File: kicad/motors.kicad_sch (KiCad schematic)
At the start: 18 parts, among them U1 DRV8848, U2 DRV8848, U3 DRV8848

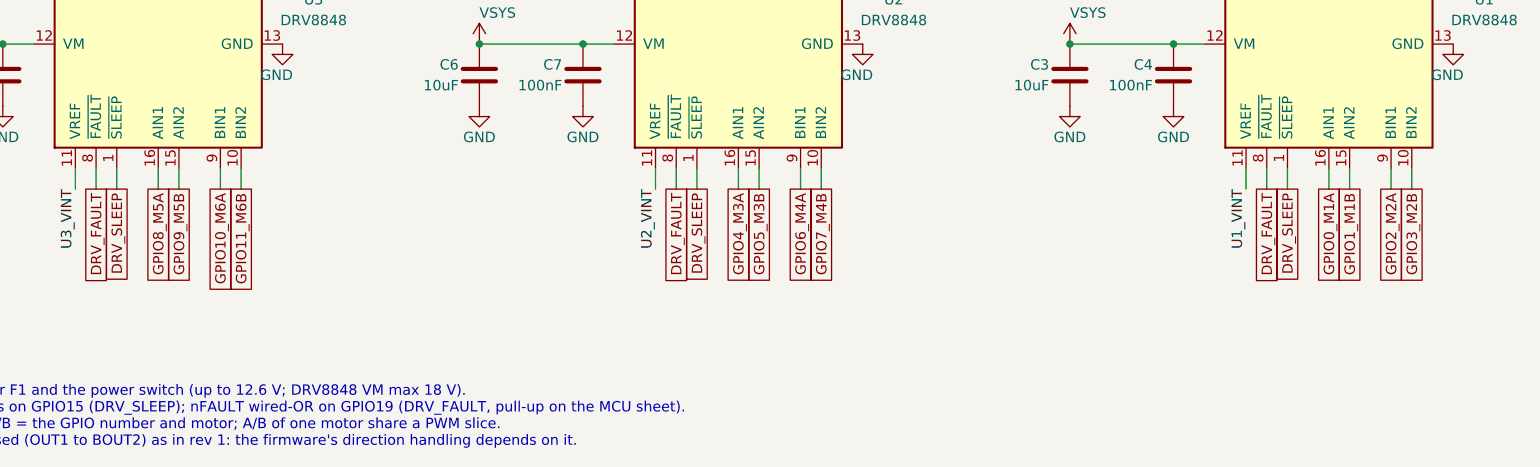
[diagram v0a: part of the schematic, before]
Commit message: Lay out rev 2 with an internal pack, protector and cost-down parts
Board is 91 x 47 mm for a 96 x 52 mm enclosure, with placement and hand
power routing done; signal routing is still to do.

- Internal Gens Ace 3S 1000 mAh pack on an XT60 pigtail, protected on the
  board by a BQ7791501 with back-to-back low-side FETs and a 2.5 mOhm
  shunt, plus a balance header and two NTCs.
- USB-A and USB-C on the top edge, IO as a recessed 3 x 6 pin block, GPIO
  map re-swapped for the placement, USB nets renamed with P/N suffixes
  for the diff-pair router.
- Cost-down swaps that keep every feature: basic or preferred passives
  and ICs, cheaper connectors, a THT power switch rated for 12.6 V, and
  replacements for the low-stock TH1 and Q2/Q3. L3 is Digi-Key sourced
  and hand-placed.
- Net classes and design rules, rev 2 power-net widths in review.py, and
  the PCB critic and loop updated for rev 2.

Schematic review passes; PCB review passes every gate except unrouted.

Co-Authored-By: Claude Opus 5.5 <noreply@anthropic.com>
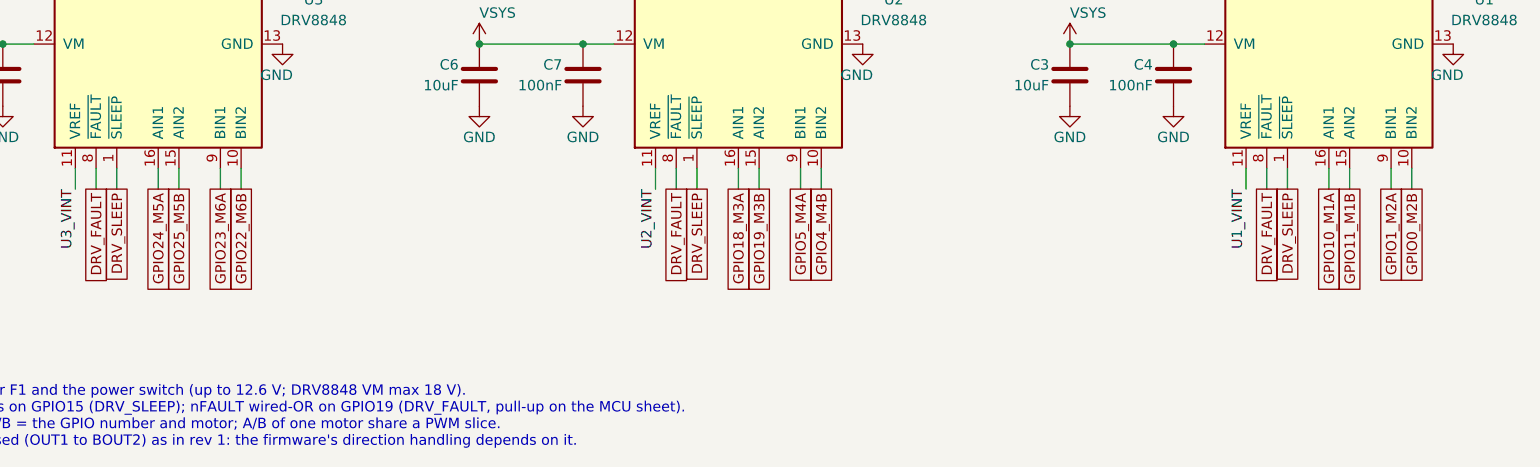
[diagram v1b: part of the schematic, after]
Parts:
- C13, C2, C9: footprint Capacitor_SMD:C_0805_2012Metric -> Capacitor_SMD:C_0603_1608Metric; LCSC Part # C377773 -> C23630; MPN CL21A225KBQNNNE -> CL10A225KO8NNNC
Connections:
- net GPIO0_M1A renamed GPIO10_M1A
- net GPIO10_M6A renamed GPIO23_M6A
- net GPIO11_M6B renamed GPIO22_M6B
- net GPIO1_M1B renamed GPIO11_M1B
- net GPIO2_M2A renamed GPIO1_M2A
- net GPIO3_M2B renamed GPIO0_M2B
- net GPIO4_M3A renamed GPIO18_M3A
- net GPIO5_M3B renamed GPIO19_M3B
- net GPIO6_M4A renamed GPIO5_M4A
- net GPIO7_M4B renamed GPIO4_M4B
- net GPIO8_M5A renamed GPIO24_M5A
- net GPIO9_M5B renamed GPIO25_M5B
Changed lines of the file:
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@@
 			)
 		)
-		(property "Footprint" "Capacitor_SMD:C_0805_2012Metric"
+		(property "Footprint" "Capacitor_SMD:C_0603_1608Metric"
 			(at 219.71 37.795199999999994 0)
 			(effects
@@
 			)
 		)
-		(property "LCSC Part #" "C377773"
+		(property "LCSC Part #" "C23630"
 			(at 251.4601 -187.9601 0)
 			(effects
@@
 			)
 		)
-    (property "MPN" "CL21A225KBQNNNE" (at 223.52 36.83 0)
+    (property "MPN" "CL10A225KO8NNNC" (at 223.52 36.83 0)
       (effects (font (size 1.27 1.27)) (hide yes))
     )
@@
 			)
 		)
-		(property "Footprint" "Capacitor_SMD:C_0805_2012Metric"
+		(property "Footprint" "Capacitor_SMD:C_0603_1608Metric"
 			(at 147.32 37.795199999999994 0)
 			(effects
@@
 			)
 		)
-		(property "LCSC Part #" "C377773"
+		(property "LCSC Part #" "C23630"
 			(at 179.0701 -115.5701 0)
 			(effects
@@
 			)
 		)
-    (property "MPN" "CL21A225KBQNNNE" (at 151.13 36.83 0)
+    (property "MPN" "CL10A225KO8NNNC" (at 151.13 36.83 0)
       (effects (font (size 1.27 1.27)) (hide yes))
     )
@@
 			)
 		)
-		(property "Footprint" "Capacitor_SMD:C_0805_2012Metric"
+		(property "Footprint" "Capacitor_SMD:C_0603_1608Metric"
 			(at 76.2 37.795199999999994 0)
 			(effects
@@
 			)
 		)
-		(property "LCSC Part #" "C377773"
+		(property "LCSC Part #" "C23630"
 			(at 107.9501 -44.450100000000006 0)
 			(effects
@@
 			)
 		)
-    (property "MPN" "CL21A225KBQNNNE" (at 80.01 36.83 0)
+    (property "MPN" "CL10A225KO8NNNC" (at 80.01 36.83 0)
       (effects (font (size 1.27 1.27)) (hide yes))
     )
@@
 	)
 	(embedded_fonts no)
-	(global_label "GPIO0_M1A"
+	(global_label "GPIO10_M1A"
 		(at 238.76 69.85 270)
 		(effects
@@
 		)
 	)
-	(global_label "GPIO1_M1B"
+	(global_label "GPIO11_M1B"
 		(at 241.3 69.85 270)
 		(effects
@@
 		)
 	)
-	(global_label "GPIO2_M2A"
+	(global_label "GPIO1_M2A"
 		(at 246.38 69.85 270)
 		(effects
@@
 		)
 	)
-	(global_label "GPIO3_M2B"
+	(global_label "GPIO0_M2B"
 		(at 248.92 69.85 270)
 		(effects
@@
 		)
 	)
-	(global_label "GPIO4_M3A"
+	(global_label "GPIO18_M3A"
 		(at 166.37 69.85 270)
 		(effects
@@
 		)
 	)
-	(global_label "GPIO5_M3B"
+	(global_label "GPIO19_M3B"
 		(at 168.91 69.85 270)
 		(effects
@@
 		)
 	)
-	(global_label "GPIO6_M4A"
+	(global_label "GPIO5_M4A"
 		(at 173.99 69.85 270)
 		(effects
@@
 		)
 	)
-	(global_label "GPIO7_M4B"
+	(global_label "GPIO4_M4B"
 		(at 176.53 69.85 270)
 		(effects
@@
 		)
 	)
-	(global_label "GPIO8_M5A"
+	(global_label "GPIO24_M5A"
 		(at 95.25 69.85 270)
 		(effects
@@
 		)
 	)
-	(global_label "GPIO9_M5B"
+	(global_label "GPIO25_M5B"
 		(at 97.79 69.85 270)
 		(effects
@@
 		)
 	)
-	(global_label "GPIO10_M6A"
+	(global_label "GPIO23_M6A"
 		(at 102.87 69.85 270)
 		(effects
@@
 		)
 	)
-	(global_label "GPIO11_M6B"
+	(global_label "GPIO22_M6B"
 		(at 105.41 69.85 270)
 		(effects

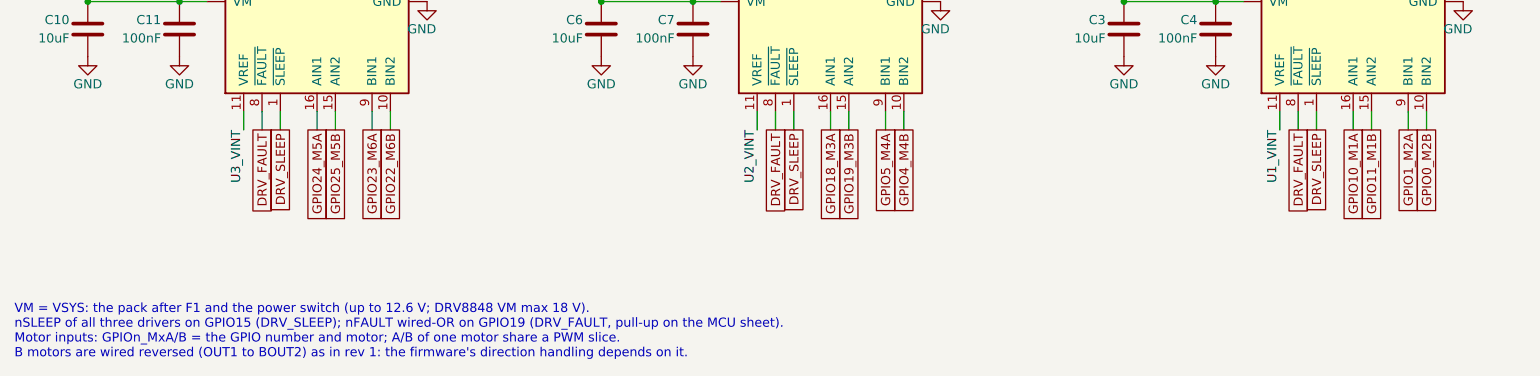
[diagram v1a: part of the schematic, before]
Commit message: Re-lay out rev 2 around an Ovonic 450 pack on top of the board
The internal pack is now an Ovonic 3S 450 mAh XT30 pack sitting 2 mm
above the board over the low-power logic area, on an XT30 pigtail. The
board is 88.5 x 47 mm with 2 mm corner radii, for a box of about
93.5 x 52 x 24.6 mm whose face has no openings.

- IO S1-S6 are a 3 x 6 right-angle header out of the left end, beside
  M5/M6, replacing the recessed vertical block.
- BOOT is a side-push switch on the top edge behind a pinhole sized for
  a 2.5 mm hex key; RESET is removed, with RUN on a bottom test pad
  beside SWCLK/SWDIO/GND.
- The CHG LED is a side-view part on the top edge; the GPIO status LED
  is removed now that the WS2812B stick shows status.
- The pack NTC is removed (a fixed 10k holds the charger's TS at 25 C);
  the protector's on-board TH1 stays.
- Q1, F1 and the other warm parts moved out from under the pack, and the
  GPIO map was re-swapped for the new placement (I2C on I2C1).

Schematic review passes; PCB review passes every gate except unrouted.

Co-Authored-By: Claude Opus 5.5 <noreply@anthropic.com>
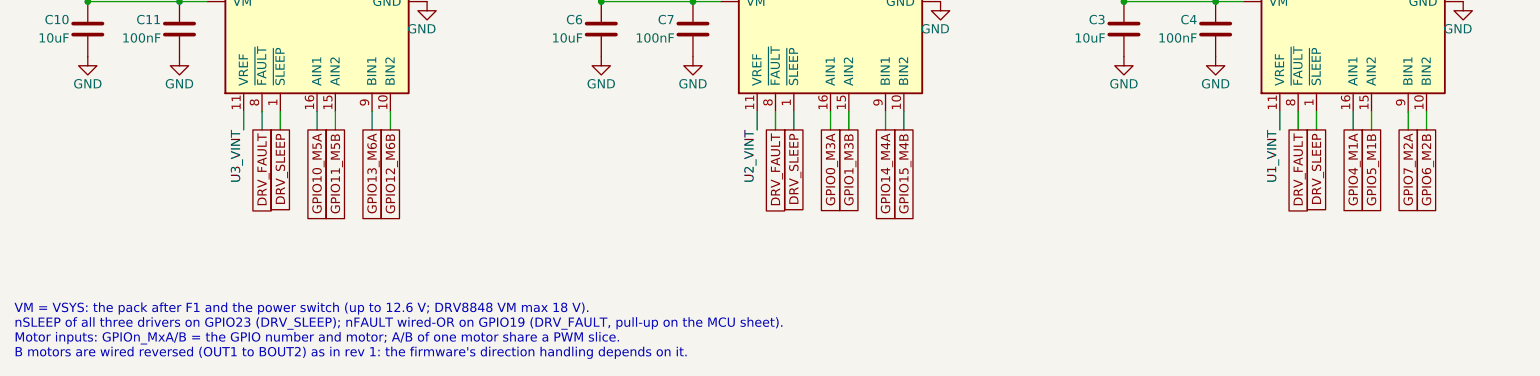
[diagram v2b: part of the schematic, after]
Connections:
- net GPIO0_M2B renamed GPIO6_M2B
- net GPIO10_M1A renamed GPIO4_M1A
- net GPIO11_M1B renamed GPIO5_M1B
- net GPIO18_M3A renamed GPIO0_M3A
- net GPIO19_M3B renamed GPIO1_M3B
- net GPIO1_M2A renamed GPIO7_M2A
- net GPIO22_M6B renamed GPIO12_M6B
- net GPIO23_M6A renamed GPIO13_M6A
- net GPIO24_M5A renamed GPIO10_M5A
- net GPIO25_M5B renamed GPIO11_M5B
- net GPIO4_M4B renamed GPIO15_M4B
- net GPIO5_M4A renamed GPIO14_M4A
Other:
- note added: "VM = VSYS: the pack after F1 and the power switch (up to 12.6 V; DRV8848 VM max 18 V). nSLEEP of all three drivers on GPIO23 (DRV_SLEEP); nFAULT wired-OR on GPIO19 (DRV_FAULT, pull-up on the MCU sheet). Motor inputs: GPIOn_MxA/B = the GPIO number and motor; A/B of one motor share a PWM slice. B motors are wired reversed (OUT1 to BOUT2) as in rev 1: the firmware's direction handling depends on it."
- note removed: "VM = VSYS: the pack after F1 and the power switch (up to 12.6 V; DRV8848 VM max 18 V). nSLEEP of all three drivers on GPIO15 (DRV_SLEEP); nFAULT wired-OR on GPIO19 (DRV_FAULT, pull-up on the MCU sheet). Motor inputs: GPIOn_MxA/B = the GPIO number and motor; A/B of one motor share a PWM slice. B motors are wired reversed (OUT1 to BOUT2) as in rev 1: the firmware's direction handling depends on it."
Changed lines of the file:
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@@
 	)
 	(embedded_fonts no)
-	(global_label "GPIO10_M1A"
+	(global_label "GPIO4_M1A"
 		(at 238.76 69.85 270)
 		(effects
@@
 		)
 	)
-	(global_label "GPIO11_M1B"
+	(global_label "GPIO5_M1B"
 		(at 241.3 69.85 270)
 		(effects
@@
 		)
 	)
-	(global_label "GPIO1_M2A"
+	(global_label "GPIO7_M2A"
 		(at 246.38 69.85 270)
 		(effects
@@
 		)
 	)
-	(global_label "GPIO0_M2B"
+	(global_label "GPIO6_M2B"
 		(at 248.92 69.85 270)
 		(effects
@@
 		)
 	)
-	(global_label "GPIO18_M3A"
+	(global_label "GPIO0_M3A"
 		(at 166.37 69.85 270)
 		(effects
@@
 		)
 	)
-	(global_label "GPIO19_M3B"
+	(global_label "GPIO1_M3B"
 		(at 168.91 69.85 270)
 		(effects
@@
 		)
 	)
-	(global_label "GPIO5_M4A"
+	(global_label "GPIO14_M4A"
 		(at 173.99 69.85 270)
 		(effects
@@
 		)
 	)
-	(global_label "GPIO4_M4B"
+	(global_label "GPIO15_M4B"
 		(at 176.53 69.85 270)
 		(effects
@@
 		)
 	)
-	(global_label "GPIO24_M5A"
+	(global_label "GPIO10_M5A"
 		(at 95.25 69.85 270)
 		(effects
@@
 		)
 	)
-	(global_label "GPIO25_M5B"
+	(global_label "GPIO11_M5B"
 		(at 97.79 69.85 270)
 		(effects
@@
 		)
 	)
-	(global_label "GPIO23_M6A"
+	(global_label "GPIO13_M6A"
 		(at 102.87 69.85 270)
 		(effects
@@
 		)
 	)
-	(global_label "GPIO22_M6B"
+	(global_label "GPIO12_M6B"
 		(at 105.41 69.85 270)
 		(effects
@@
 		)
 	)
-	(text "VM = VSYS: the pack after F1 and the power switch (up to 12.6 V; DRV8848 VM max 18 V).\nnSLEEP of all three drivers on GPIO15 (DRV_SLEEP); nFAULT wired-OR on GPIO19 (DRV_FAULT, pull-up on the MCU sheet).\nMotor inputs: GPIOn_MxA/B = the GPIO number and motor; A/B of one motor share a PWM slice.\nB motors are wired reversed (OUT1 to BOUT2) as in rev 1: the firmware's direction handling depends on it."
+	(text "VM = VSYS: the pack after F1 and the power switch (up to 12.6 V; DRV8848 VM max 18 V).\nnSLEEP of all three drivers on GPIO23 (DRV_SLEEP); nFAULT wired-OR on GPIO19 (DRV_FAULT, pull-up on the MCU sheet).\nMotor inputs: GPIOn_MxA/B = the GPIO number and motor; A/B of one motor share a PWM slice.\nB motors are wired reversed (OUT1 to BOUT2) as in rev 1: the firmware's direction handling depends on it."
 		(exclude_from_sim no)
 		(at 53.34 93.98 0)
